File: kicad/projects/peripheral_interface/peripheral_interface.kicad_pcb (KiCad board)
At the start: 2 copper layers, 203.2 x 97.8 mm, 41 parts, among them J1 Pi Pico Standin, J2 VOLTAGE CONVERTER, J3 OLED SCREEN, J4 BACKPLANE AUX, J5 BACKPLANE BANK, J6 BACKPLANE BUS, J7 TO CPU, J8 FROM CPU, J9 KEYPAD, U1 74HC595, U10 74HC597, U11 74HCT157, U12 74HCT157, U13 74HCT245, U14 74HC597, U2 74HC595, U3 74HC595, U4 74HC595, U5 74HC595, U6 74HC595, U7 74HC597, U8 74HC597, U9 74HC597

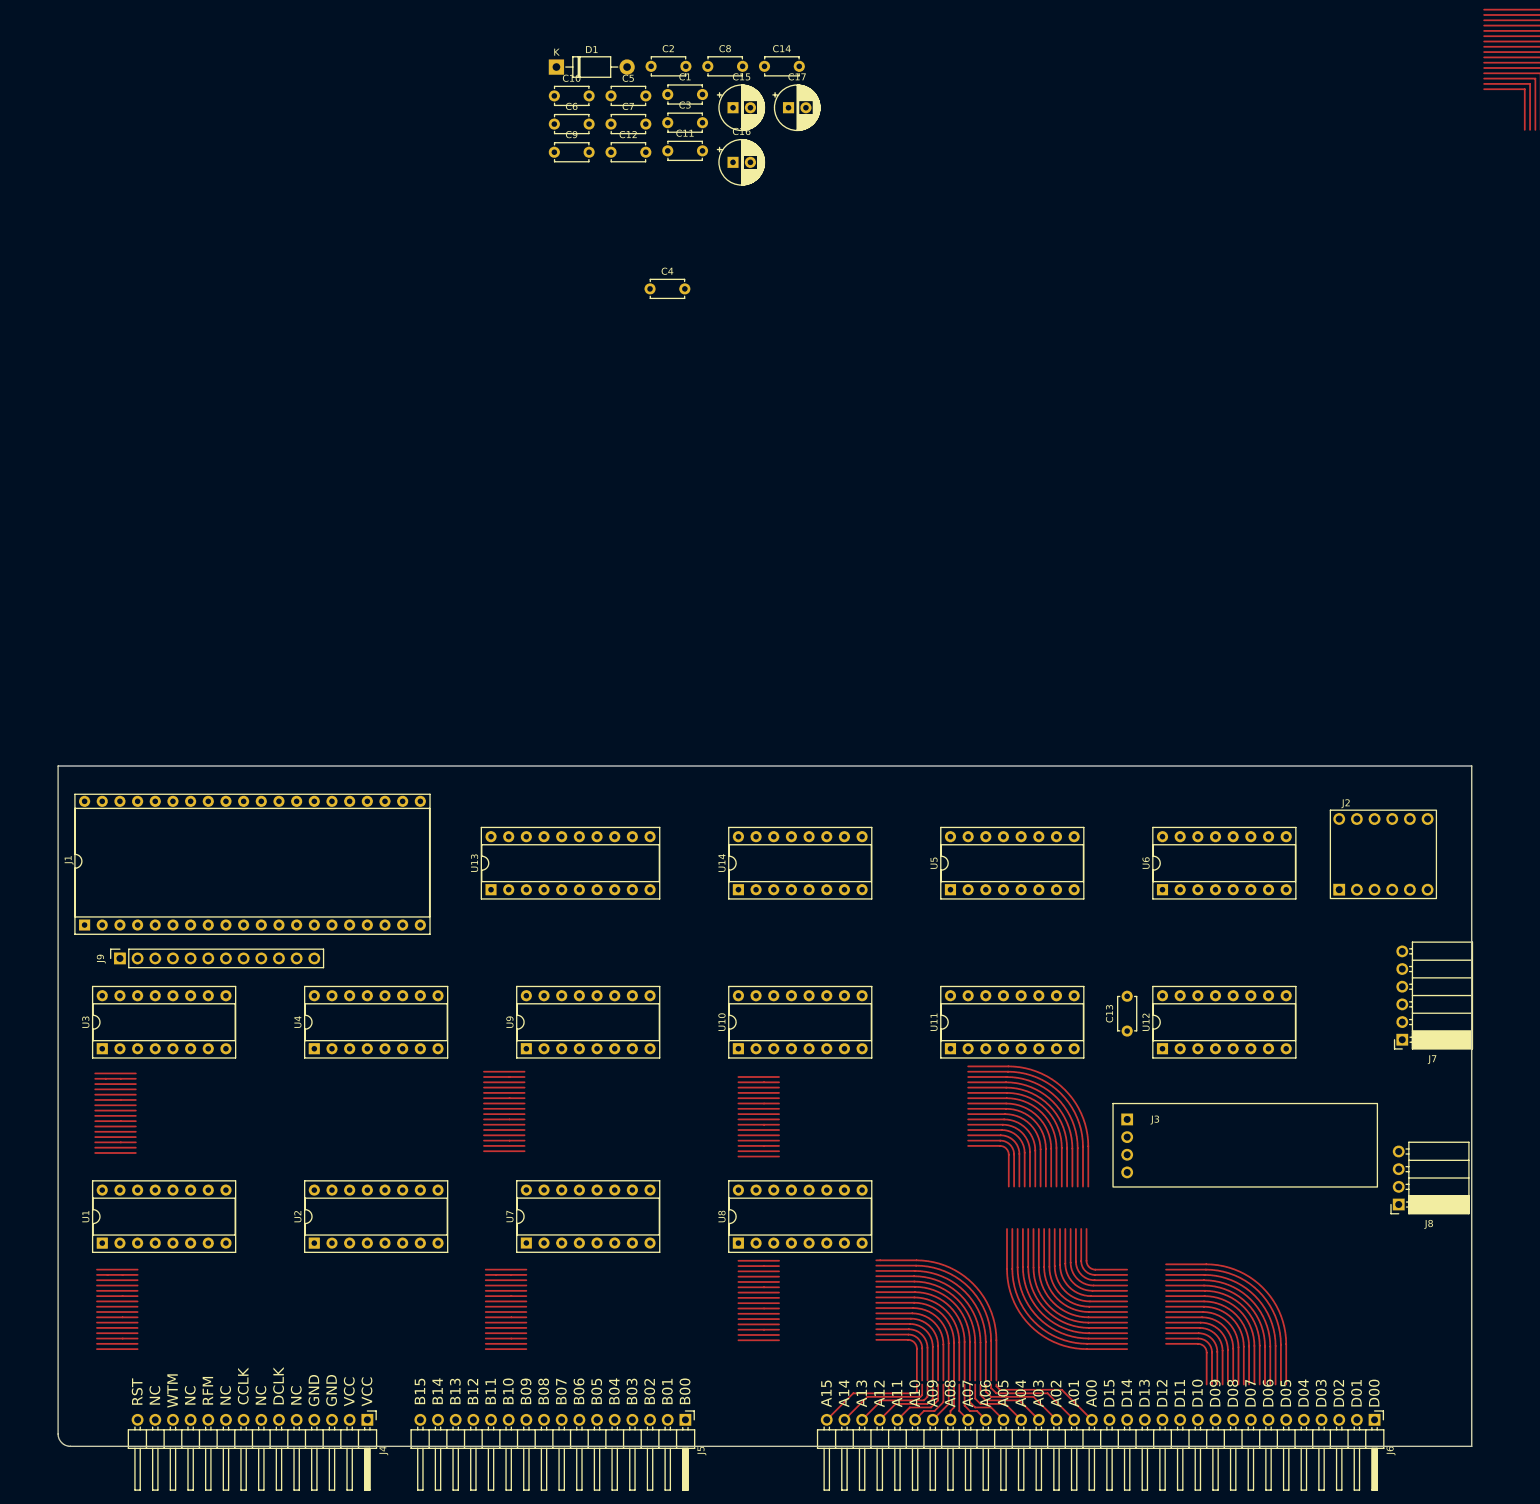
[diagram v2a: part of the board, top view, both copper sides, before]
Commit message: Start laying out PCB and upgrade to KiCad 7.
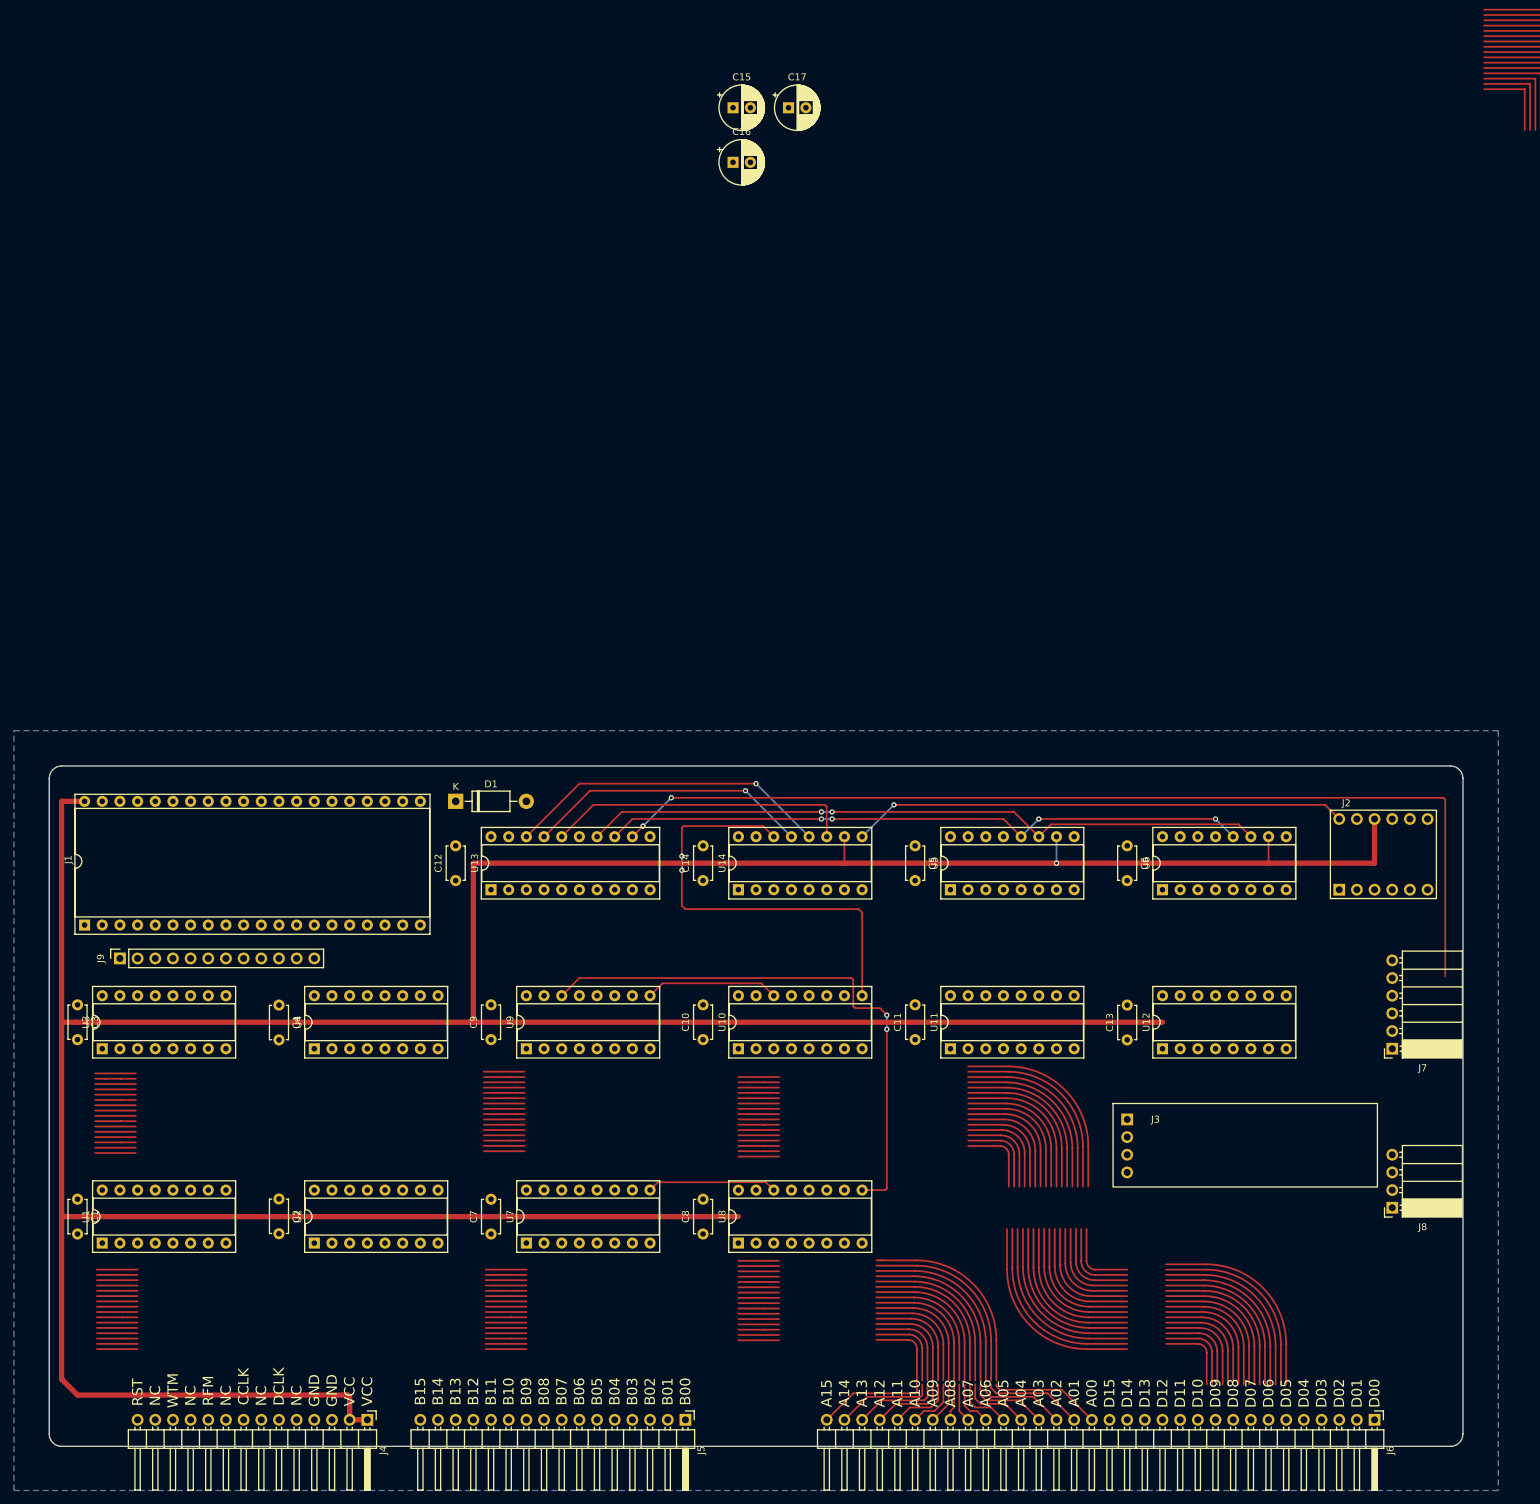
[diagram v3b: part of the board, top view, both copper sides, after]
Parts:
- moved C1 180.0 mm to (57.4, 108.0), turned to -90 degrees
- moved C2 171.4 mm to (86.4, 108.0), turned to -90 degrees
- moved C8 167.8 mm to (147.3, 113.0), turned to 90 degrees
- moved C7 160.5 mm to (116.8, 113.0), turned to 90 degrees
- moved C3 152.6 mm to (57.4, 80.0), turned to -90 degrees
- moved C10 137.3 mm to (147.3, 85.0), turned to 90 degrees
- moved C11 132.6 mm to (177.8, 85.0), turned to 90 degrees
- moved C6 132.4 mm to (208.3, 57.2), turned to -90 degrees
- moved C9 127.9 mm to (116.8, 85.0), turned to 90 degrees
- moved C14 117.4 mm to (147.3, 62.2), turned to 90 degrees
- moved C5 116.3 mm to (177.8, 57.2), turned to -90 degrees
- moved C4 115.9 mm to (86.4, 80.1), turned to -90 degrees
- moved C12 107.0 mm to (111.8, 62.2), turned to 90 degrees
- moved D1 106.5 mm to (111.8, 50.8)
- moved J7 1.94 mm to (246.4, 86.4)
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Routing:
- net VCC: track 0.00 -> 561.1 mm, vias 0 -> 1
- net (no net): track 2526.5 -> 2203.9 mm
- net /CLK_PULSE_5V: track 0.00 -> 144.7 mm, vias 0 -> 2
- net /SERIAL_WRITE_SHIFT_CLK_5V: track 0.00 -> 98.4 mm, vias 0 -> 2
- net /SERIAL_WRITE_OUT_CLK_5V: track 0.00 -> 93.1 mm, vias 0 -> 4
- net Net-(U8-Pad9): track 0.00 -> 80.8 mm, vias 0 -> 2
- net /SERIAL_READ_DATA_5V: track 0.00 -> 71.3 mm, vias 0 -> 1
- net Net-(U10-Pad9): track 0.00 -> 63.4 mm, vias 0 -> 2
- net /SERIAL_READ_STORAGE_CLK_5V: track 0.00 -> 47.0 mm, vias 0 -> 1
- net /SERIAL_READ_SHIFT_CLK_5V: track 0.00 -> 44.4 mm
- net /SERIAL_READ_PARALLEL_LOAD_5V: track 0.00 -> 41.0 mm, vias 0 -> 1
- net /ADDR_BUS_00: track 16.0 -> 45.1 mm
- net /ADDR_BUS_01: track 14.3 -> 42.3 mm
- net /ADDR_BUS_02: track 12.9 -> 39.6 mm
- net /ADDR_BUS_03: track 11.4 -> 36.9 mm
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- added copper zone on B.Cu, net GND
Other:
- outline, holes or cut-outs redrawn

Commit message: Bit more work on peripheral interface PCB.
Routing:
- net /3V3_FROM_PICO: track 0.00 -> 286.3 mm, vias 0 -> 4
- net /SERIAL_READ_DATA_3V3: track 0.00 -> 152.0 mm
- net /SERIAL_WRITE_DATA_5V: track 0.25 -> 124.3 mm, vias 0 -> 4
- net /SERIAL_WRITE_OUT_CLK_5V: track 93.1 -> 214.2 mm, vias 4 -> 7
- net /SERIAL_WRITE_SHIFT_CLK_5V: track 98.4 -> 217.1 mm, vias 2 -> 4
- net /ADDR_BUS_00: track 45.1 -> 154.2 mm
- net /ADDR_BUS_01: track 42.3 -> 151.4 mm
- net /ADDR_BUS_02: track 39.6 -> 148.5 mm
- net /ADDR_BUS_03: track 36.9 -> 145.7 mm
- net /ADDR_BUS_04: track 34.2 -> 142.8 mm
- net /ADDR_BUS_05: track 31.6 -> 140.0 mm
- net /ADDR_BUS_06: track 29.0 -> 137.1 mm
- net /ADDR_BUS_07: track 26.4 -> 134.3 mm
- net /ADDR_BUS_08: track 25.0 -> 131.4 mm
- net /ADDR_BUS_09: track 24.5 -> 128.5 mm
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
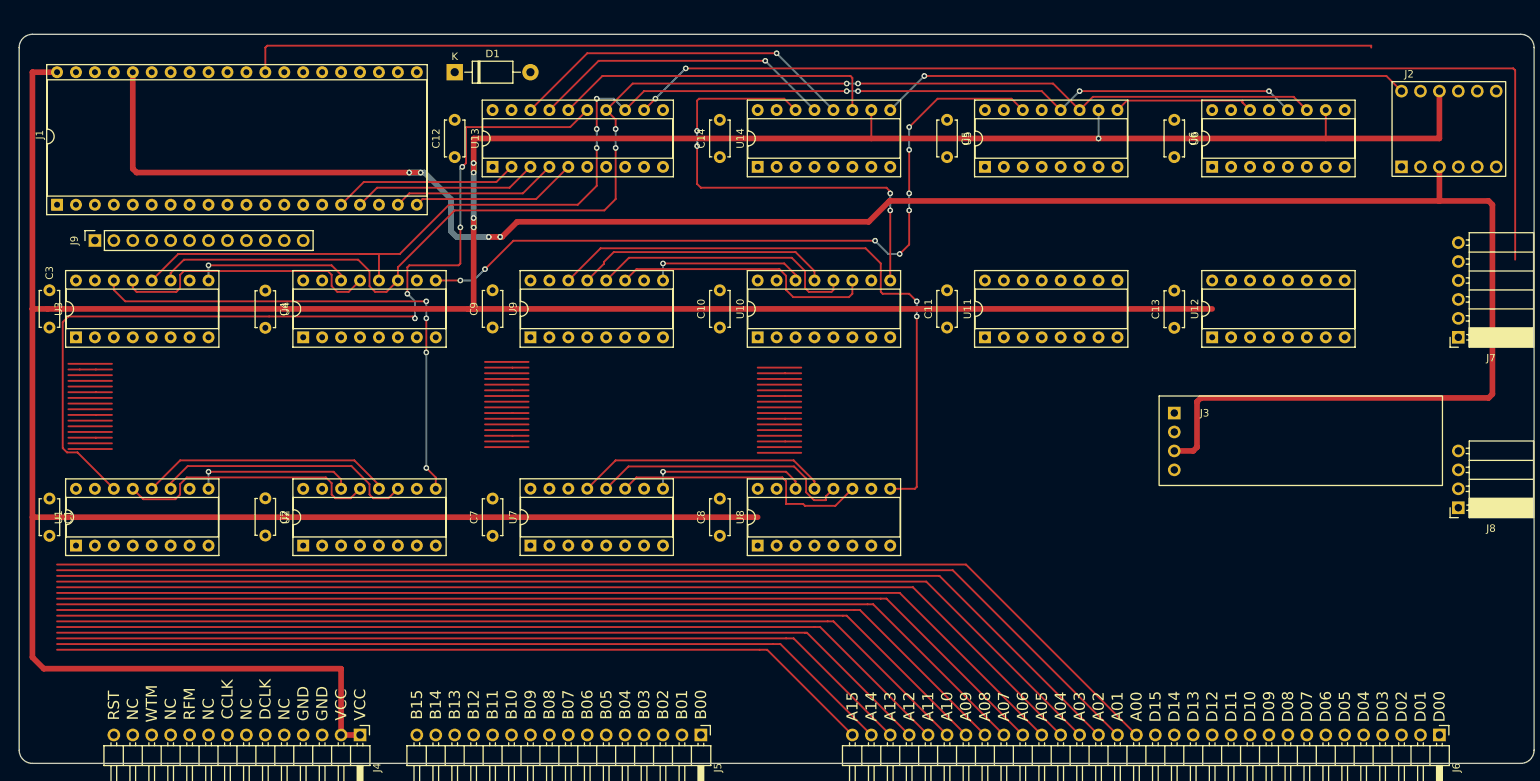
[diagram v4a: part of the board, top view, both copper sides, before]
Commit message: More work on peripheral PCB. Added seperate reset lines for CPU and peripherals.
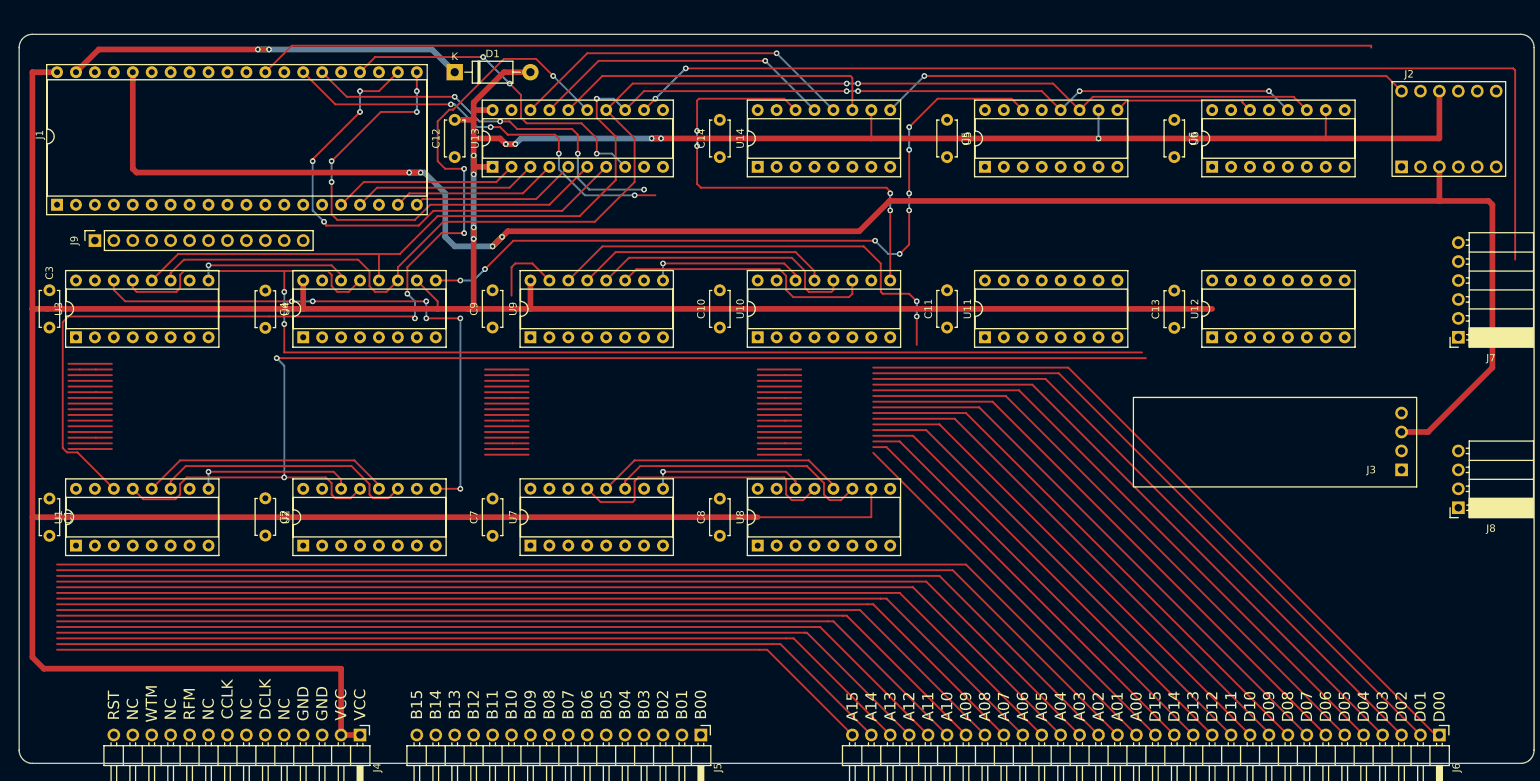
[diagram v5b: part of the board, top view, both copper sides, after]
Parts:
- moved J3 31.4 mm to (238.8, 104.1), turned to 180 degrees
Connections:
- J4 pad 14: /RESET -> /RESET_TO_PERIPH
- J7 pad 6: /RESET -> /RESET_TO_CPU
- U6 pad 15: /RESET -> /RESET_TO_CPU
- U6 pad 5: unconnected-(U6-Pad5) -> /RESET_TO_PERIPH
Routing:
- net /INTERFACE_ADDR_ASSERT: track 35.7 -> 168.7 mm, vias 0 -> 2
- net /INTERFACE_DATA_ASSERT: track 36.6 -> 162.6 mm, vias 0 -> 2
- net /DATA_BUS_00: track 0.00 -> 96.4 mm
- net /DATA_BUS_01: track 0.00 -> 93.5 mm
- net /DATA_BUS_02: track 0.00 -> 90.6 mm
- net /DATA_BUS_03: track 0.00 -> 87.8 mm
- net /DATA_BUS_04: track 0.00 -> 84.9 mm
- net /DATA_BUS_05: track 0.00 -> 82.1 mm
- net /DATA_BUS_06: track 0.00 -> 79.2 mm
- net /DATA_BUS_07: track 0.00 -> 77.1 mm
- net /DATA_BUS_08: track 0.00 -> 73.5 mm
- net /DATA_BUS_09: track 0.00 -> 70.8 mm
- net /SERIAL_WRITE_OUT_CLK_3V3: track 0.00 -> 68.4 mm, vias 0 -> 4
- net /DATA_BUS_10: track 0.00 -> 67.8 mm
- net /DATA_BUS_11: track 0.00 -> 64.9 mm
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
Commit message: More work on peripheral PCB.
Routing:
- net /SCREEN_SDA: track 53.1 -> 145.1 mm
- net /SCREEN_SCL: track 56.5 -> 147.0 mm
- net /DATA_CLK_FROM_CPU: track 0.00 -> 76.2 mm
- net /CTL_CLK_FROM_CPU: track 0.00 -> 73.8 mm
- net VCC: track 622.4 -> 693.3 mm, vias 9 -> 28
- net /RFM_FROM_CPU: track 0.00 -> 67.6 mm, vias 0 -> 4
- net /WTM_FROM_CPU: track 0.00 -> 57.8 mm, vias 0 -> 2
- net /RESET_TO_CPU: track 0.00 -> 44.8 mm, vias 0 -> 2
- net /DATA_CLK_FROM_IFCE: track 0.00 -> 44.0 mm
- net /CTL_CLK_FROM_IFCE: track 0.00 -> 35.2 mm
- net /INTERFACE_ADDR_ASSERT: track 168.7 -> 203.5 mm, vias 2 -> 6
- net /RFM_AND_WTM_SEL: track 0.00 -> 33.2 mm, vias 0 -> 2
- net /DATA_AND_CTL_CLK_SEL: track 0.00 -> 33.0 mm, vias 0 -> 2
- net /INTERFACE_DATA_ASSERT: track 162.6 -> 193.9 mm, vias 2 -> 6
- net /RESET_TO_PERIPH: track 0.00 -> 28.4 mm
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
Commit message: More work on peripheral PCB.
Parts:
- moved J7 15.2 mm to (246.4, 101.6)
- moved J8 14.0 mm to (246.4, 123.2)
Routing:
- net /CLK_EN_TO_CPU: track 0.00 -> 54.7 mm
- net /ADDR_OE_TO_CPU: track 0.00 -> 54.1 mm, vias 0 -> 2
- net /CLK_SEL_TO_CPU: track 0.00 -> 50.2 mm
- net /DATA_OE_TO_CPU: track 0.00 -> 49.5 mm, vias 0 -> 2
- net /RESET_TO_PERIPH: track 28.4 -> 76.7 mm, vias 0 -> 2
- net /SCREEN_SDA: track 145.1 -> 185.8 mm
- net /SCREEN_SCL: track 147.0 -> 184.8 mm, vias 4 -> 6
- net /CLK_PULSE_5V: track 144.7 -> 167.6 mm
- net /CTL_CLK_FROM_IFCE: track 35.2 -> 55.3 mm, vias 0 -> 2
- net /CTL_CLK_FROM_CPU: track 73.8 -> 92.4 mm, vias 0 -> 2
- net /RFM_FROM_CPU: track 67.6 -> 86.0 mm, vias 4 -> 6
- net VCC: track 693.3 -> 711.1 mm
- net /RFM: track 17.3 -> 34.7 mm, vias 0 -> 1
- net /DATA_CLK_FROM_IFCE: track 44.0 -> 60.8 mm, vias 0 -> 2
- net /DATA_CLK_FROM_CPU: track 76.2 -> 91.5 mm, vias 0 -> 2
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
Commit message: Routing on Periph interface complete.
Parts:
- removed C17: C_Polarized, Capacitor_THT:CP_Radial_D6.3mm_P2.50mm
- moved C15 206.2 mm to (58.2, 134.9), turned to -90 degrees
- moved C16 149.2 mm to (250.4, 70.9), turned to 180 degrees
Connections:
- J1 pad 40: VCC -> unconnected-(J1-VBUS-Pad40)
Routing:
- net (no net): track 2246.1 -> 0.00 mm
- net /DATA_CLK: track 6.03 -> 169.8 mm, vias 0 -> 6
- net /RESET_TO_PERIPH: track 76.7 -> 239.8 mm, vias 2 -> 8
- net /CONTROL_CLK: track 11.6 -> 174.1 mm, vias 0 -> 6
- net /WTM: track 29.8 -> 181.5 mm, vias 1 -> 5
- net /RFM: track 34.7 -> 184.8 mm, vias 1 -> 5
- net /DATA_BUS_07: track 76.3 -> 217.9 mm, vias 0 -> 5
- net /DATA_BUS_15: track 86.6 -> 224.2 mm, vias 2 -> 8
- net /DATA_BUS_14: track 56.3 -> 187.7 mm, vias 0 -> 1
- net /DATA_BUS_13: track 59.1 -> 186.9 mm, vias 0 -> 1
- net /DATA_BUS_12: track 62.0 -> 186.1 mm, vias 0 -> 1
- net /DATA_BUS_11: track 64.8 -> 185.4 mm, vias 0 -> 1
- net /DATA_BUS_10: track 67.7 -> 184.6 mm, vias 0 -> 1
- net /DATA_BUS_09: track 70.7 -> 184.0 mm, vias 0 -> 1
- net /DATA_BUS_08: track 73.4 -> 183.1 mm, vias 0 -> 1
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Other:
- board text added: "ADDR OE"
- board text added: "CLK EN"
- board text added: "CLK PULSE"
- board text added: "CLK SEL"
- board text added: "CTL CLK"
- board text added: "DATA CLK"
- board text added: "DATA OE"
- board text added: "RESET"
- board text added: "RFM"
- board text added: "WTM"
